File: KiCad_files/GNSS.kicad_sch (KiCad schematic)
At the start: 1 part

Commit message: GNSS aloitettu
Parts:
- added C10: 2.2u, symbol Device:C
- added C11, C12, C13, C14, C9: 22p, symbol Device:C
- added L1, L2: 47n, symbol Device:L
- added L3: 1.8n, symbol Device:L
- added R9: 0, symbol Device:R
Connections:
- net at U10.1 (AT1): now also R9.2
- net HW_R: now reaches U10.10 (HW_R)
- net TM: now reaches U10.11 (TM)
- net at U10.12 (BV): now also C9.1
- net E1_BAUD_SELECT: now reaches U10.13 (E2)
- net E2_BAUD_SELECT: now reaches U10.14 (E3)
- net GND: now reaches U10.15 (GND)
- net GND: now also U10.16 (GND), U10.17 (GND), U10.19 (GND), U10.2 (GND), U10.20 (TX), U10.22 (GND), U10.23 (GND), U10.24 (GND), U10.25 (GND), U10.27 (GND), U10.3 (GND), U10.5 (GND), U10.7 (GND), U10.9 (GND), C10.2, C11.2, C12.2, C13.2, C9.2, L2.1, L3.2, R9.1
- net FIX: now reaches U10.18 (FIX)
- net at U10.21 (RX): now also L1.1
- net HW_S: now reaches U10.26 (HW_S)
- net at U10.28 (AT2): now also L3.1
- net at U10.4 (ANT_OUT): now also C14.1
- net at U10.6 (RF_IN): now also C14.2
- net +3.3V: now reaches U10.8 (VCC)
- net +3.3V: now also C10.1, C11.1
- new net RX: C12.1, L1.2
- new net TX: C13.1, L2.2
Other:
- note added: "Baud select. NC = not connected, PD = pull down BAUD RATE E2 E3 9600 NC NC 115200 NC PD 4800 PD NC 38400 PD PD"
- note added: "Could probably use this to determine whether to include the GPS data into the sensor fusion"
- note added: "Decoupling caps from ref"
- note added: "FIX signal indicates whether the module has a fix on the position. In other words, if it has locked onto enough satellites that it can determine the position. Can't tell by the datasheet what it outputs. Probably just 0 or 1"
- note added: "Hardware controlled standby. Enable standby by sending a low state to this pin. To wake up, send high state to this pin. If not used, leave floating!"
- note added: "Hardware reset pin. If not used, the hardware reset should be left floating, as it is pulled up by an internal 75 k resistor"
- note added: "Pulse per second output, which provides a synchronized output which is synchronized to GNSS time. Pulse width is 100 ms. Enable with command PMTK255"
- note added: "Standby mode command via software: Software on the host needs to send the "PMTK161" command through the UART interface."
- note added: "TODO: Backup voltage. Need a 3 volt battery to enable quick startup and satellite acquisition by the GPS Do other devices require this as well?"
- note added: "TODO: Tuning inductor and resistor are TBD Need to research how to determine their values. These vals are from the reference schematic"
- note added: "TODO: find out WTF is this shit"
- note added: "UART interface. Cross-connect with MCU: RX -> TX, TX -> RX Select baud rate with pins E2 & E3"

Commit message: GNSS aloitettu
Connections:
- net GND: no longer L2.1, U10.20 (TX)
- new net: L2.1, U10.20 (TX)
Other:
- note added: "Pulse per second output, which provides a synchronized output which is synchronized to GNSS time. Pulse width is 100 ms. Enable with command PMTK255 Leave floating if not needed"
- note removed: "Pulse per second output, which provides a synchronized output which is synchronized to GNSS time. Pulse width is 100 ms. Enable with command PMTK255"
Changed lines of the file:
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@@
 		)
 	)
-	(text "Pulse per second output, which provides a synchronized\noutput which is synchronized to GNSS time.\nPulse width is 100 ms. Enable with command PMTK255 "
+	(text "Pulse per second output, which provides a synchronized\noutput which is synchronized to GNSS time.\nPulse width is 100 ms. Enable with command PMTK255 \n\nLeave floating if not needed"
 		(exclude_from_sim no)
-		(at 41.402 115.062 0)
+		(at 42.672 116.84 0)
 		(effects
 			(font
@@
 	)
 	(junction
+		(at 160.02 106.68)
+		(diameter 0)
+		(color 0 0 0 0)
+	)
+	(junction
 		(at 137.16 119.38)
 		(diameter 0)
@@
 	)
 	(junction
-		(at 160.02 106.68)
+		(at 106.68 88.9)
+		(diameter 0)
+		(color 0 0 0 0)
+	)
+	(junction
+		(at 160.02 93.98)
+		(diameter 0)
+		(color 0 0 0 0)
+	)
+	(junction
+		(at 127 165.1)
+		(diameter 0)
+		(color 0 0 0 0)
+	)
+	(junction
+		(at 203.2 104.14)
+		(diameter 0)
+		(color 0 0 0 0)
+	)
+	(junction
+		(at 63.5 63.5)
 		(diameter 0)
 		(color 0 0 0 0)
@@
 		(color 0 0 0 0)
 	)
-	(junction
-		(at 106.68 88.9)
-		(diameter 0)
-		(color 0 0 0 0)
-	)
-	(junction
-		(at 160.02 104.14)
-		(diameter 0)
-		(color 0 0 0 0)
-	)
-	(junction
-		(at 160.02 93.98)
-		(diameter 0)
-		(color 0 0 0 0)
-	)
-	(junction
-		(at 127 165.1)
-		(diameter 0)
-		(color 0 0 0 0)
-	)
-	(junction
-		(at 203.2 104.14)
-		(diameter 0)
-		(color 0 0 0 0)
-	)
-	(junction
-		(at 63.5 63.5)
-		(diameter 0)
-		(color 0 0 0 0)
-	)
 	(wire
 		(pts
@@
 	(wire
 		(pts
-			(xy 156.21 104.14) (xy 160.02 104.14)
+			(xy 156.21 104.14) (xy 193.04 104.14)
 		)
 		(stroke
@@
 	(wire
 		(pts
-			(xy 160.02 104.14) (xy 160.02 106.68)
-		)
-		(stroke
-			(width 0)
-			(type default)
-		)
-	)
-	(wire
-		(pts
 			(xy 50.8 63.5) (xy 63.5 63.5)
 		)
@@
 	(wire
 		(pts
+			(xy 160.02 99.06) (xy 160.02 106.68)
+		)
+		(stroke
+			(width 0)
+			(type default)
+		)
+	)
+	(wire
+		(pts
 			(xy 134.62 116.84) (xy 134.62 119.38)
 		)
@@
 	(wire
 		(pts
-			(xy 160.02 104.14) (xy 193.04 104.14)
-		)
-		(stroke
-			(width 0)
-			(type default)
-		)
-	)
-	(wire
-		(pts
 			(xy 177.8 62.23) (xy 177.8 63.5)
 		)
@@
 		)
 		(stroke
-			(width 0)
-			(type default)
-		)
-	)
-	(wire
-		(pts
-			(xy 160.02 99.06) (xy 160.02 104.14)
-		)
-		(stroke

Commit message: GNSS WIP
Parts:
- added BT1: 3 V, symbol Device:Battery_Cell
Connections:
- net GND: now also BT1.2 (-)
- net at C9.1, U10.12 (BV): now also BT1.1 (+)
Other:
- note added: "Backup voltage. Need a 3 volt battery to enable quick startup and satellite acquisition by the GPS TODO: Do other devices require this as well?"
- note added: "Could probably use this to determine whether to include the GPS data into the sensor fusion if(FIX) do readgps()"
- note added: "UART interface. Cross-connect with MCU: RX -> TX, TX -> RX Select baud rate with pins E2 & E3 OR via software"
- note removed: "Could probably use this to determine whether to include the GPS data into the sensor fusion"
- note removed: "TODO: Backup voltage. Need a 3 volt battery to enable quick startup and satellite acquisition by the GPS Do other devices require this as well?"
- note removed: "UART interface. Cross-connect with MCU: RX -> TX, TX -> RX Select baud rate with pins E2 & E3"
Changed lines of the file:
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@@
 	(generator_version "9.0")
 	(paper "A4")
-	(text "TODO: Backup voltage. Need a 3 volt battery to enable\nquick startup and satellite acquisition by the GPS\n\nDo other devices require this as well?\n"
-		(exclude_from_sim no)
-		(at 94.488 173.228 0)
+	(text "Backup voltage. Need a 3 volt battery to enable\nquick startup and satellite acquisition by the GPS\n\nTODO: Do other devices require this as well?\n"
+		(exclude_from_sim no)
+		(at 59.182 177.546 0)
 		(effects
 			(font
@@
 		)
 	)
-	(text "Could probably use this to determine whether to\ninclude the GPS data into the sensor fusion"
+	(text "Could probably use this to determine whether to\ninclude the GPS data into the sensor fusion\nif(FIX) do readgps()"
 		(exclude_from_sim no)
 		(at 248.92 145.034 0)
@@
 		)
 	)
-	(text "UART interface. Cross-connect with MCU:\nRX -> TX, TX -> RX\nSelect baud rate with pins E2 & E3"
+	(text "UART interface. Cross-connect with MCU:\nRX -> TX, TX -> RX\nSelect baud rate with pins E2 & E3 \nOR via software"
 		(exclude_from_sim no)
 		(at 243.84 102.87 0)
@@
 	(wire
 		(pts
+			(xy 88.9 165.1) (xy 88.9 177.8)
+		)
+		(stroke
+			(width 0)
+			(type default)
+		)
+	)
+	(wire
+		(pts
 			(xy 93.98 99.06) (xy 93.98 97.79)
 		)
@@
 	(wire
 		(pts
+			(xy 104.14 165.1) (xy 88.9 165.1)
+		)
+		(stroke
+			(width 0)
+			(type default)
+		)
+	)
+	(wire
+		(pts
 			(xy 165.1 139.7) (xy 215.9 139.7)
 		)
@@
 	(wire
 		(pts
-			(xy 93.98 165.1) (xy 127 165.1)
+			(xy 111.76 165.1) (xy 127 165.1)
 		)
 		(stroke
@@
 					(unit 1)
 				)
+			)
+		)
+	)
+	(symbol
+		(lib_id "Device:Battery_Cell")
+		(at 106.68 165.1 270)
+		(unit 1)
+		(exclude_from_sim no)
+		(in_bom yes)
+		(on_board yes)
+		(dnp no)
+		(fields_autoplaced yes)
+		(property "Reference" "BT1"
+			(at 108.5215 157.48 90)
+			(effects
+				(font
+					(size 1.27 1.27)
+				)
+			)
+		)
+		(property "Value" "3 V"
+			(at 108.5215 160.02 90)
+			(effects
+				(font
+					(size 1.27 1.27)
+				)
+			)
+		)
+		(property "Footprint" ""
+			(at 108.204 165.1 90)
+			(effects
+				(font
+					(size 1.27 1.27)
+				)
+				(hide yes)
+			)
+		)
+		(property "Datasheet" "~"
+			(at 108.204 165.1 90)
+			(effects
+				(font
+					(size 1.27 1.27)
+				)
+				(hide yes)
+			)
+		)
+		(property "Description" "Single-cell battery"
+			(at 106.68 165.1 0)
+			(effects
+				(font
+					(size 1.27 1.27)
+				)
+				(hide yes)
+			)
+		)
+		(property "Sim.Device" "V"
+			(at 106.68 165.1 0)
+			(effects
+				(font
+					(size 1.27 1.27)
+				)
+				(hide yes)
+			)
+		)
+		(property "Sim.Type" "DC"
+			(at 106.68 165.1 0)
+			(effects
+				(font
+					(size 1.27 1.27)
+				)
+				(hide yes)
+			)
+		)
+		(property "Sim.Pins" "1=+ 2=-"
+			(at 106.68 165.1 0)
+			(effects
+				(font
+					(size 1.27 1.27)
+				)
+				(hide yes)
+			)
+		)
+		(pin "1"
+		)
+		(pin "2"
+		)
+		(instances
+			(project ""
+				(path "/186d5500-054c-4b47-a89c-85f6ce2abe33/58061273-0348-4c5f-98ae-c78a02c73d37"
+					(reference "BT1")
+					(unit 1)
+				)
+			)
+		)
+	)
+	(symbol
+		(lib_id "power:GND")
+		(at 88.9 177.8 0)
+		(unit 1)
+		(exclude_from_sim no)
+		(in_bom yes)
+		(on_board yes)
+		(dnp no)
+		(fields_autoplaced yes)
+		(property "Reference" "#PWR040"
+			(at 88.9 184.15 0)
+			(effects
+				(font
+					(size 1.27 1.27)
+				)
+				(hide yes)
+			)
+		)
+		(property "Value" "GND"
+			(at 88.9 182.88 0)
+			(effects
+				(font
+					(size 1.27 1.27)
+				)
+			)
+		)
+		(property "Footprint" ""
+			(at 88.9 177.8 0)
+			(effects
+				(font
+					(size 1.27 1.27)
+				)
+				(hide yes)
+			)
+		)
+		(property "Datasheet" ""
+			(at 88.9 177.8 0)
+			(effects
+				(font
+					(size 1.27 1.27)
+				)
+				(hide yes)
+			)
+		)
+		(property "Description" "Power symbol creates a global label with name \"GND\" , ground"
+			(at 88.9 177.8 0)
+			(effects
+				(font
+					(size 1.27 1.27)
+				)
+				(hide yes)
+			)
+		)
+		(pin "1"
+		)
+		(instances
+			(project ""
+				(path "/186d5500-054c-4b47-a89c-85f6ce2abe33/58061273-0348-4c5f-98ae-c78a02c73d37"
+					(reference "#PWR040")
+					(unit 1)
+				)

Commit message: footprinttejä
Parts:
- U10: footprint (none) -> 1_project_library:QFN28_M20048-1_ANT
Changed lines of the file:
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@@
 			)
 		)
-		(property "Footprint" ""
+		(property "Footprint" "1_project_library:QFN28_M20048-1_ANT"
 			(at 113.03 78.74 0)
 			(effects

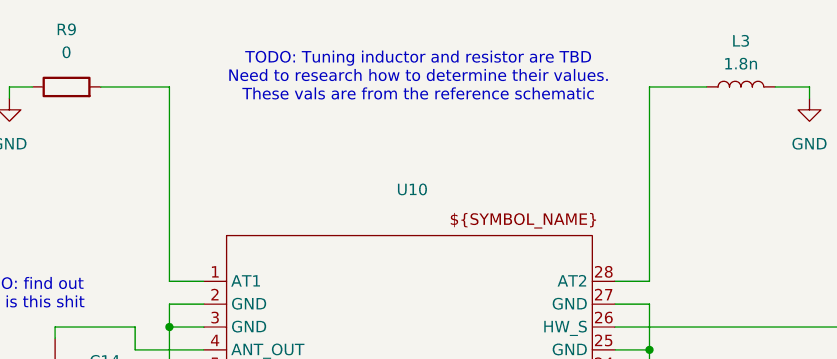
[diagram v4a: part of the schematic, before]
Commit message: footprinttejä komponenteille + kapasitanssit korjattu imusta
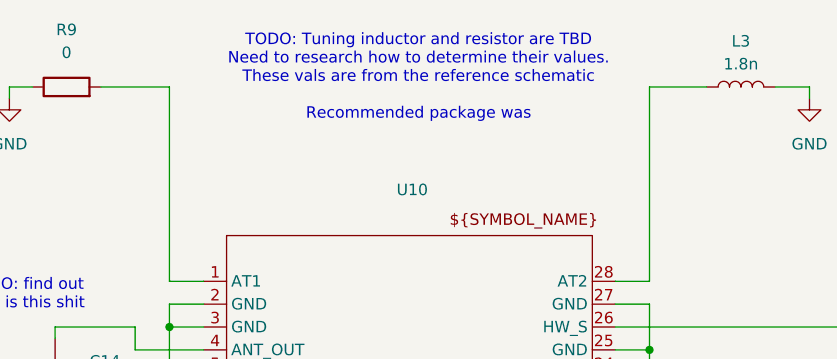
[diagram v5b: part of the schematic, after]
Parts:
- C10, C11, C12, C13, C14, C9: footprint (none) -> Capacitor_SMD:C_0805_2012Metric_Pad1.18x1.45mm_HandSolder
- R9: footprint (none) -> Resistor_SMD:R_0805_2012Metric_Pad1.20x1.40mm_HandSolder
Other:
- note added: "TODO: Tuning inductor and resistor are TBD Need to research how to determine their values. These vals are from the reference schematic Recommended package was"
- note removed: "TODO: Tuning inductor and resistor are TBD Need to research how to determine their values. These vals are from the reference schematic"
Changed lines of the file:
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@@
 		)
 	)
-	(text "TODO: Tuning inductor and resistor are TBD\nNeed to research how to determine their values.\nThese vals are from the reference schematic"
+	(text "TODO: Tuning inductor and resistor are TBD\nNeed to research how to determine their values.\nThese vals are from the reference schematic\n\nRecommended package was"
 		(exclude_from_sim no)
 		(at 134.366 61.214 0)
@@
 			)
 		)
-		(property "Footprint" ""
+		(property "Footprint" "Capacitor_SMD:C_0805_2012Metric_Pad1.18x1.45mm_HandSolder"
 			(at 51.7652 73.66 0)
 			(effects
@@
 			)
 		)
-		(property "Footprint" ""
+		(property "Footprint" "Capacitor_SMD:C_0805_2012Metric_Pad1.18x1.45mm_HandSolder"
 			(at 94.9452 97.79 0)
 			(effects
@@
 			)
 		)
-		(property "Footprint" ""
+		(property "Footprint" "Capacitor_SMD:C_0805_2012Metric_Pad1.18x1.45mm_HandSolder"
 			(at 204.1652 124.46 0)
 			(effects
@@
 			)
 		)
-		(property "Footprint" ""
+		(property "Footprint" "Capacitor_SMD:C_0805_2012Metric_Pad1.18x1.45mm_HandSolder"
 			(at 64.4652 73.66 0)
 			(effects
@@
 			)
 		)
-		(property "Footprint" ""
+		(property "Footprint" "Capacitor_SMD:C_0805_2012Metric_Pad1.18x1.45mm_HandSolder"
 			(at 127.9652 175.26 0)
 			(effects
@@
 			)
 		)
-		(property "Footprint" ""
+		(property "Footprint" "Resistor_SMD:R_0805_2012Metric_Pad1.20x1.40mm_HandSolder"
 			(at 95.25 64.008 90)
 			(effects
@@
 			)
 		)
-		(property "Footprint" ""
+		(property "Footprint" "Capacitor_SMD:C_0805_2012Metric_Pad1.18x1.45mm_HandSolder"
 			(at 191.4652 124.46 0)
 			(effects

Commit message: ajan tasalle
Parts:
- L1, L2: footprint (none) -> Inductor_SMD:L_0805_2012Metric_Pad1.05x1.20mm_HandSolder; DigiKey (none) -> 445-1032-1-ND
- L3: footprint (none) -> Inductor_SMD:L_0805_2012Metric_Pad1.05x1.20mm_HandSolder; DigiKey (none) -> 2035-1135-1-ND
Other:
- note added: "0805CT-1N8EJTS"
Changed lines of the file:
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@@
+		)
+	)
+	(text "0805CT-1N8EJTS"
+		(exclude_from_sim no)
+		(at 170.434 53.848 0)
+		(effects
+			(font
+				(size 1.27 1.27)
+			)
 		)
 	)
@@
 			)
 		)
-		(property "Footprint" ""
+		(property "Footprint" "Inductor_SMD:L_0805_2012Metric_Pad1.05x1.20mm_HandSolder"
 			(at 196.85 104.14 0)
 			(effects
@@
 		(property "Description" "Inductor"
 			(at 196.85 104.14 0)
+			(effects
+				(font
+					(size 1.27 1.27)
+				)
+				(hide yes)
+			)
+		)
+		(property "DigiKey" "445-1032-1-ND"
+			(at 196.85 104.14 90)
 			(effects
 				(font
@@
 			)
 		)
-		(property "Footprint" ""
+		(property "Footprint" "Inductor_SMD:L_0805_2012Metric_Pad1.05x1.20mm_HandSolder"
 			(at 170.18 62.23 0)
 			(effects
@@
 		(property "Description" "Inductor"
 			(at 170.18 62.23 0)
+			(effects
+				(font
+					(size 1.27 1.27)
+				)
+				(hide yes)
+			)
+		)
+		(property "DigiKey" "2035-1135-1-ND"
+			(at 170.18 62.23 90)
 			(effects
 				(font
@@
 			)
 		)
-		(property "Footprint" ""
+		(property "Footprint" "Inductor_SMD:L_0805_2012Metric_Pad1.05x1.20mm_HandSolder"
 			(at 184.15 101.6 0)
 			(effects
@@
 			(effects
 				(font
+					(size 1.27 1.27)
+				)
+				(hide yes)
+			)
+		)
+		(property "DigiKey" "445-1032-1-ND"
+			(at 184.15 101.6 90)
+			(effects
+				(font

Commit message: paristo lisätty
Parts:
- removed BT1: 3 V, symbol Device:Battery_Cell
- added U2: 1060, 1060_KEY, symbol 1_projektin osat:1060
- C10: DigiKey (none) -> 399-C0805C225K4RACTUCT-ND
- C11, C12, C13, C14, C9: DigiKey (none) -> 399-17625-1-ND
- R9: DigiKey (none) -> 311-0.0ARCT-ND
- U10: DigiKey (none) -> 627-1099-1-ND
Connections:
- net GND: now also U2.1
- net at C9.1, U10.12 (BV): now also U2.2
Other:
- moved on the sheet: C9

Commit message: update
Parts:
- U2: footprint 1060_KEY -> 1_project_library:1060_KEY
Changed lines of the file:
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@@
+			)
+		)
+		(property "Sim.Type" ""
+			(at 50.8 69.85 0)
+			(effects
+				(font
+					(size 1.27 1.27)
+				)
+				(hide yes)
 			)
 		)
@@
 			)
 		)
+		(property "Sim.Type" ""
+			(at 93.98 93.98 0)
+			(effects
+				(font
+					(size 1.27 1.27)
+				)
+				(hide yes)
+			)
+		)
 		(pin "2"
 		)
@@
 			)
 		)
+		(property "Sim.Type" ""
+			(at 196.85 104.14 90)
+			(effects
+				(font
+					(size 1.27 1.27)
+				)
+				(hide yes)
+			)
+		)
 		(pin "1"
 		)
@@
 			)
 		)
+		(property "Sim.Type" ""
+			(at 203.2 120.65 0)
+			(effects
+				(font
+					(size 1.27 1.27)
+				)
+				(hide yes)
+			)
+		)
 		(pin "2"
 		)
@@
 			)
 		)
+		(property "Sim.Type" ""
+			(at 63.5 69.85 0)
+			(effects
+				(font
+					(size 1.27 1.27)
+				)
+				(hide yes)
+			)
+		)
 		(pin "2"
 		)
@@
 			)
 		)
+		(property "Sim.Type" ""
+			(at 127 173.99 0)
+			(effects
+				(font
+					(size 1.27 1.27)
+				)
+				(hide yes)
+			)
+		)
 		(pin "1"
 		)
@@
 			)
 		)
+		(property "Sim.Type" ""
+			(at 95.25 62.23 90)
+			(effects
+				(font
+					(size 1.27 1.27)
+				)
+				(hide yes)
+			)
+		)
 		(pin "2"
 		)
@@
 			)
 		)
-		(property "Footprint" "1060_KEY"
+		(property "Footprint" "1_project_library:1060_KEY"
 			(at 81.28 167.64 0)
 			(effects
@@
 			)
 		)
+		(property "Sim.Type" ""
+			(at 81.28 167.64 0)
+			(effects
+				(font
+					(size 1.27 1.27)
+				)
+				(hide yes)
+			)
+		)
 		(pin "1"
 		)
@@
 			)
 		)
+		(property "Sim.Type" ""
+			(at 170.18 62.23 90)
+			(effects
+				(font
+					(size 1.27 1.27)
+				)
+				(hide yes)
+			)
+		)
 		(pin "1"
 		)
@@
 			)
 		)
+		(property "Sim.Type" ""
+			(at 113.03 78.74 0)
+			(effects
+				(font
+					(size 1.27 1.27)
+				)
+				(hide yes)
+			)
+		)
 		(pin "14"
 		)
@@
 			)
 		)
+		(property "Sim.Type" ""
+			(at 184.15 101.6 90)
+			(effects
+				(font
+					(size 1.27 1.27)
+				)
+				(hide yes)
+			)
+		)
 		(pin "1"
 		)
@@
 			(at 190.5 120.65 0)
 			(effects
+				(font
+					(size 1.27 1.27)
+				)
+				(hide yes)
+			)
+		)
+		(property "Sim.Type" ""
+			(at 190.5 120.65 0)
+			(effects
